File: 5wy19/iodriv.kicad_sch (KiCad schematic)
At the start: 4 parts, among them IC3 74HCT574, IC4 HIP0045

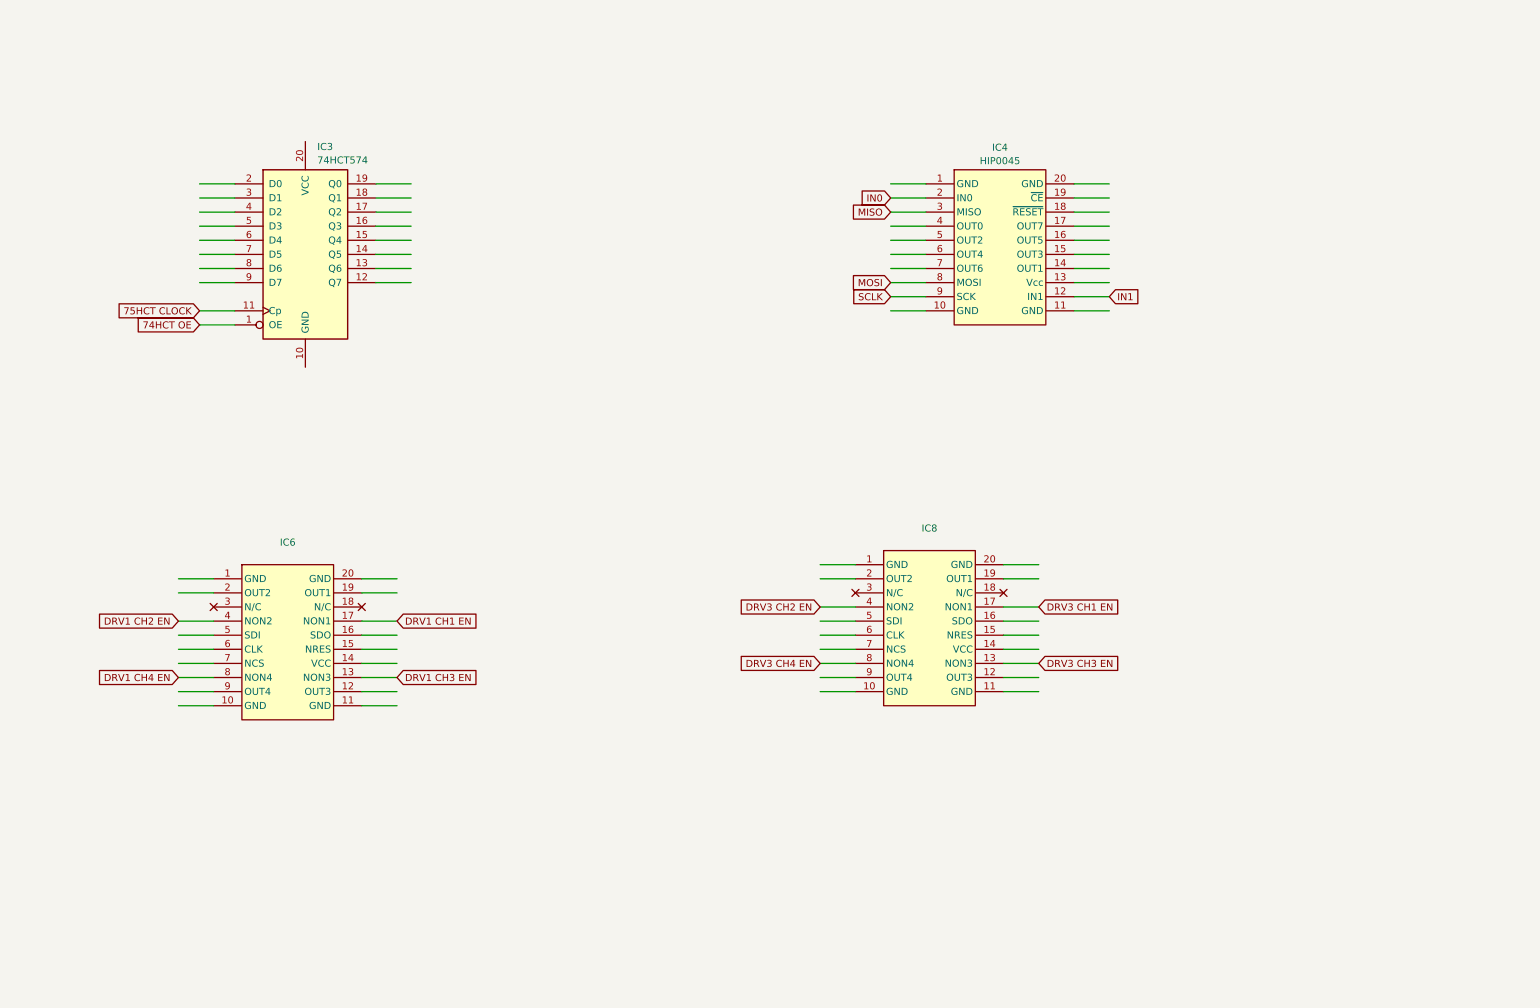
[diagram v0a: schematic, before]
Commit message: Further progress on MCU and connected circuits
Mostly sensors, knock control, some pins from the IO drivers and the unknown AMIS chip
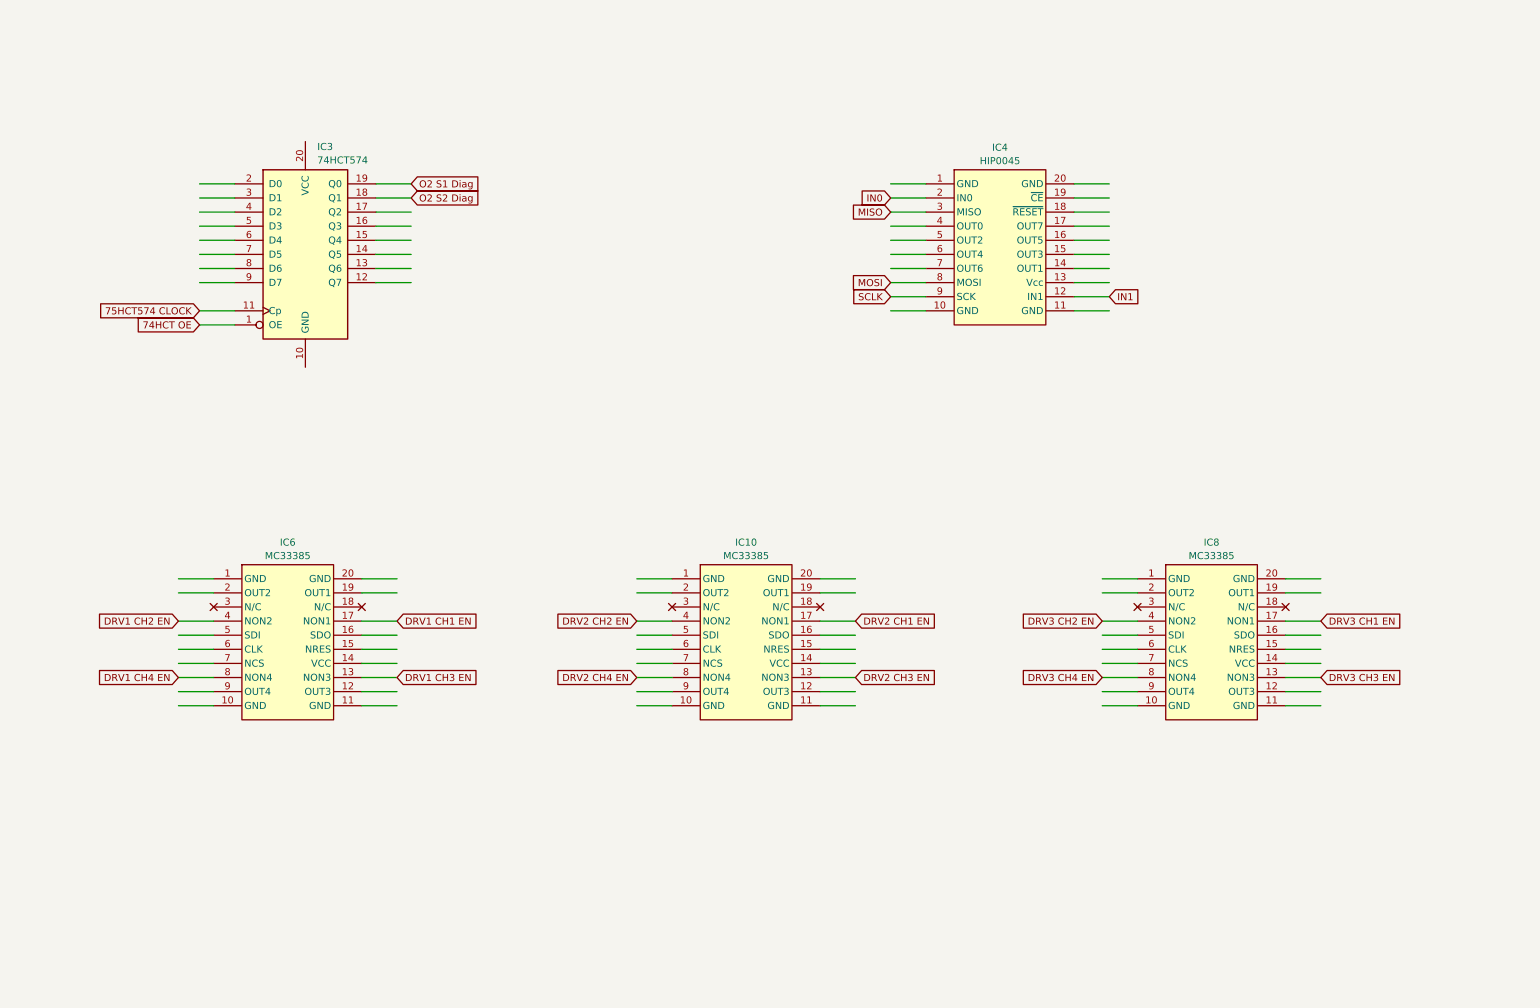
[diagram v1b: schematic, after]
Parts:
- added IC10: MC33385, symbol SIMK43:MC33385
- IC6, IC8: value ~ -> MC33385
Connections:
- net O2 S2 Diag: now reaches IC3.18 (Q1)
- net O2 S1 Diag: now reaches IC3.19 (Q0)
- net 75HCT CLOCK renamed 75HCT574 CLOCK
- new net DRV2 CH1 EN: IC10.17 (NON1)
- new net DRV2 CH2 EN: IC10.4 (NON2)
- new net DRV2 CH3 EN: IC10.13 (NON3)
- new net DRV2 CH4 EN: IC10.8 (NON4)
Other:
- moved on the sheet: IC8

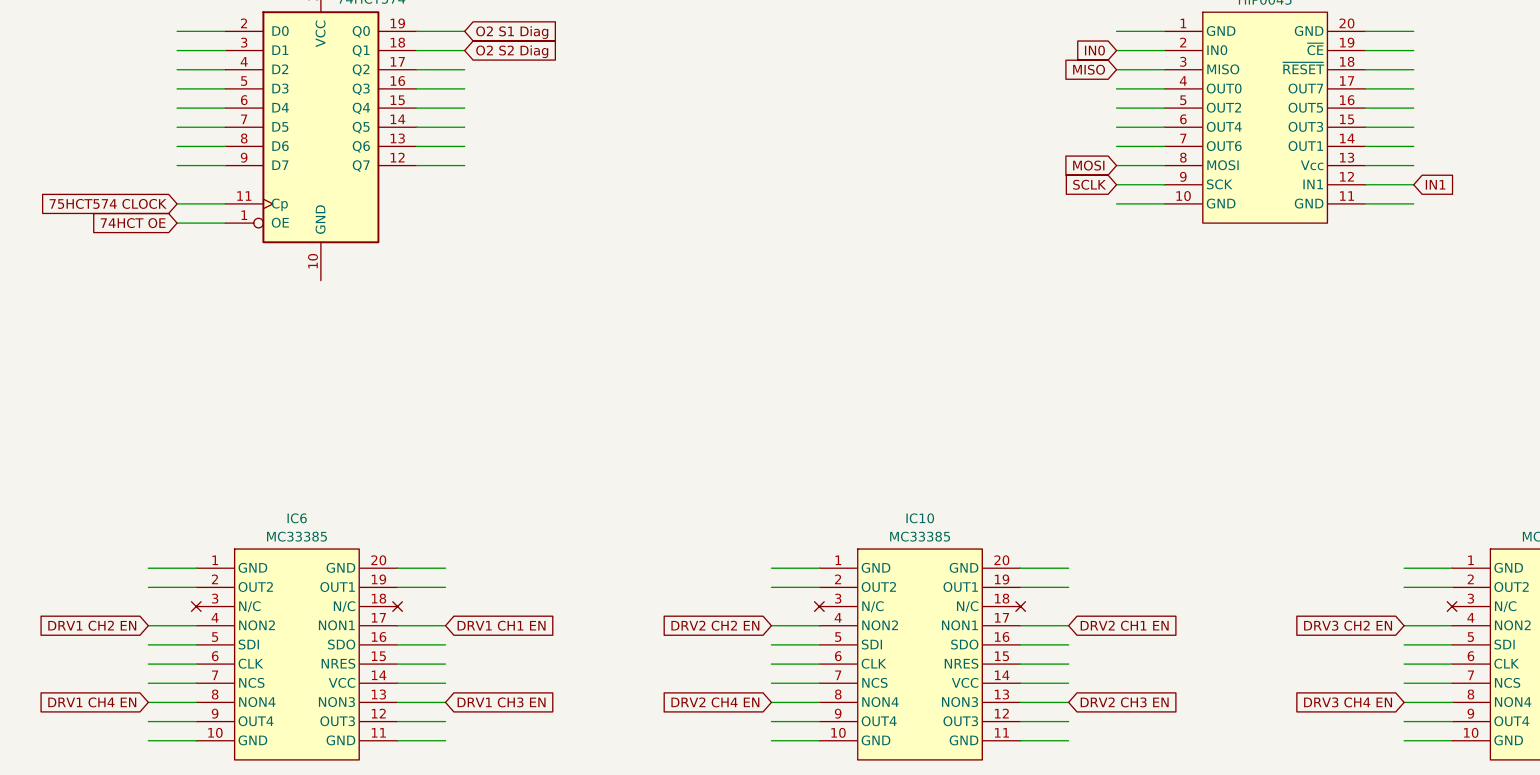
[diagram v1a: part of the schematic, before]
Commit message: Mapped out more pins of MCU and relevant circuits
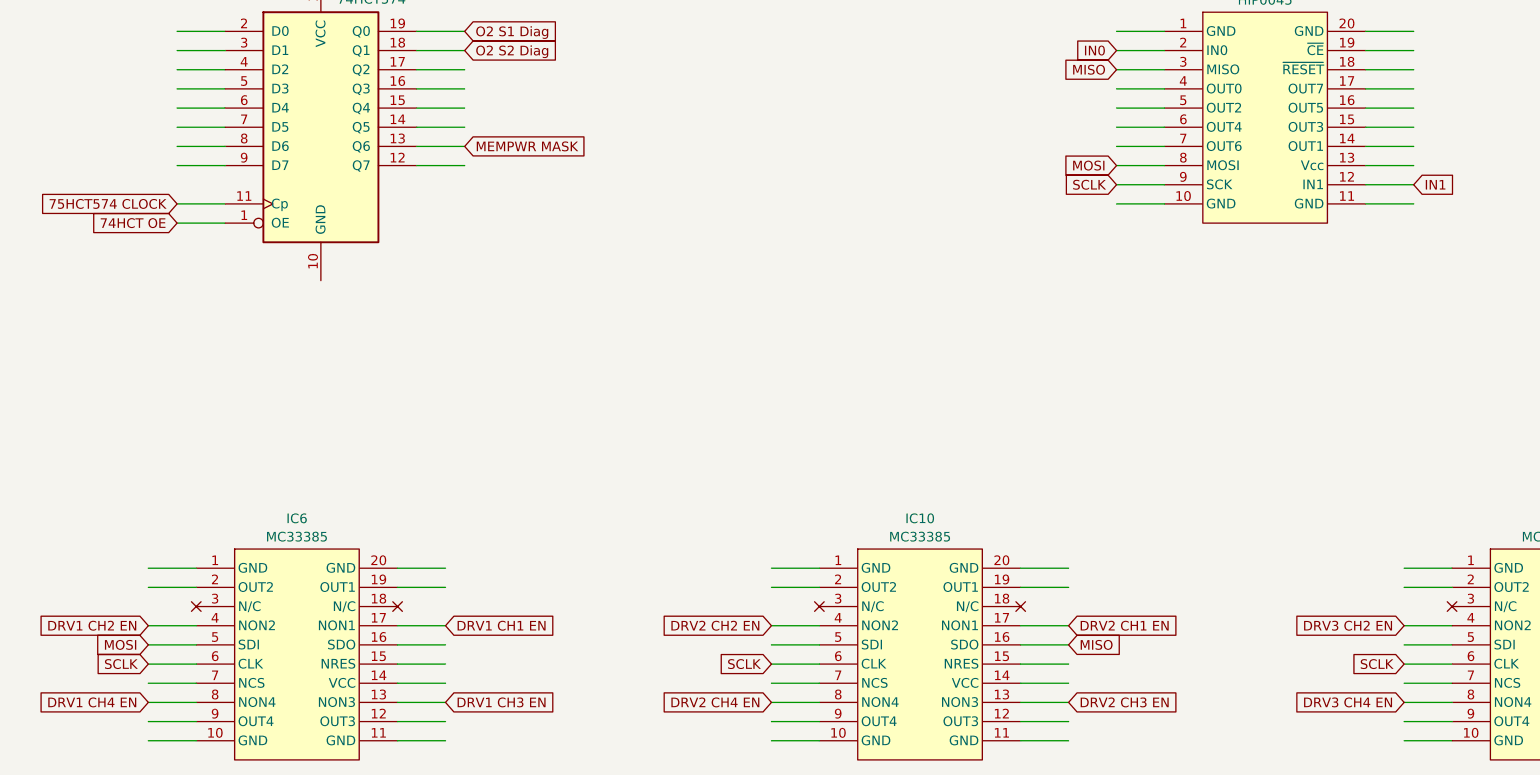
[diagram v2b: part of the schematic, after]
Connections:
- net MISO: now also IC10.16 (SDO)
- net MOSI: now also IC6.5 (SDI)
- net SCLK: now also IC10.6 (CLK), IC6.6 (CLK), IC8.6 (CLK)
- net MEMPWR MASK: now reaches IC3.13 (Q6)
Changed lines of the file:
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@@
+		)
+	)
+	(global_label "MISO"
+		(shape input)
+		(at 163.83 124.46 0)
+		(fields_autoplaced yes)
+		(effects
+			(font
+				(size 1.27 1.27)
+			)
+			(justify left)
+		)
+		(property "Intersheetrefs" "${INTERSHEET_REFS}"
+			(at 179.8779 124.46 0)
+			(effects
+				(font
+					(size 1.27 1.27)
+				)
+				(justify left)
+				(hide yes)
+			)
 		)
 	)
@@
 		)
 	)
+	(global_label "MEMPWR MASK"
+		(shape input)
+		(at 83.82 58.42 0)
+		(fields_autoplaced yes)
+		(effects
+			(font
+				(size 1.27 1.27)
+			)
+			(justify left)
+		)
+		(property "Intersheetrefs" "${INTERSHEET_REFS}"
+			(at 100.8355 58.42 0)
+			(effects
+				(font
+					(size 1.27 1.27)
+				)
+				(justify left)
+				(hide yes)
+			)
+		)
+	)
 	(global_label "DRV1 CH1 EN"
 		(shape input)
@@
 		)
 	)
+	(global_label "SCLK"
+		(shape input)
+		(at 208.28 127 180)
+		(fields_autoplaced yes)
+		(effects
+			(font
+				(size 1.27 1.27)
+			)
+			(justify right)
+		)
+		(property "Intersheetrefs" "${INTERSHEET_REFS}"
+			(at 200.5172 127 0)
+			(effects
+				(font
+					(size 1.27 1.27)
+				)
+				(justify right)
+				(hide yes)
+			)
+		)
+	)
 	(global_label "DRV1 CH4 EN"
 		(shape input)
@@
 		)
 	)
+	(global_label "SCLK"
+		(shape input)
+		(at 124.46 127 180)
+		(fields_autoplaced yes)
+		(effects
+			(font
+				(size 1.27 1.27)
+			)
+			(justify right)
+		)
+		(property "Intersheetrefs" "${INTERSHEET_REFS}"
+			(at 116.6972 127 0)
+			(effects
+				(font
+					(size 1.27 1.27)
+				)
+				(justify right)
+				(hide yes)
+			)
+		)
+	)
+	(global_label "MOSI"
+		(shape input)
+		(at 41.91 124.46 180)
+		(fields_autoplaced yes)
+		(effects
+			(font
+				(size 1.27 1.27)
+			)
+			(justify right)
+		)
+		(property "Intersheetrefs" "${INTERSHEET_REFS}"
+			(at 34.3286 124.46 0)
+			(effects
+				(font
+					(size 1.27 1.27)
+				)
+				(justify right)
+				(hide yes)
+			)
+		)
+	)
 	(global_label "74HCT OE"
 		(shape input)
@@
 				(hide yes)
 			)
+		)
+	)
+	(global_label "SCLK"
+		(shape input)
+		(at 41.91 127 180)
+		(fields_autoplaced yes)
+		(effects
+			(font
+				(size 1.27 1.27)
+			)
+			(justify right)
+		)
+		(property "Intersheetrefs" "${INTERSHEET_REFS}"
+			(at 34.1472 127 0)
+			(effects
+				(font
+					(size 1.27 1.27)
+				)
+				(justify right)
+				(hide yes)
+			)
